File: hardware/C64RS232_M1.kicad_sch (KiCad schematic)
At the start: 9 parts, among them J1 C64 USER PORT, J2 5747844-4, U1 MAX3243EIPWR

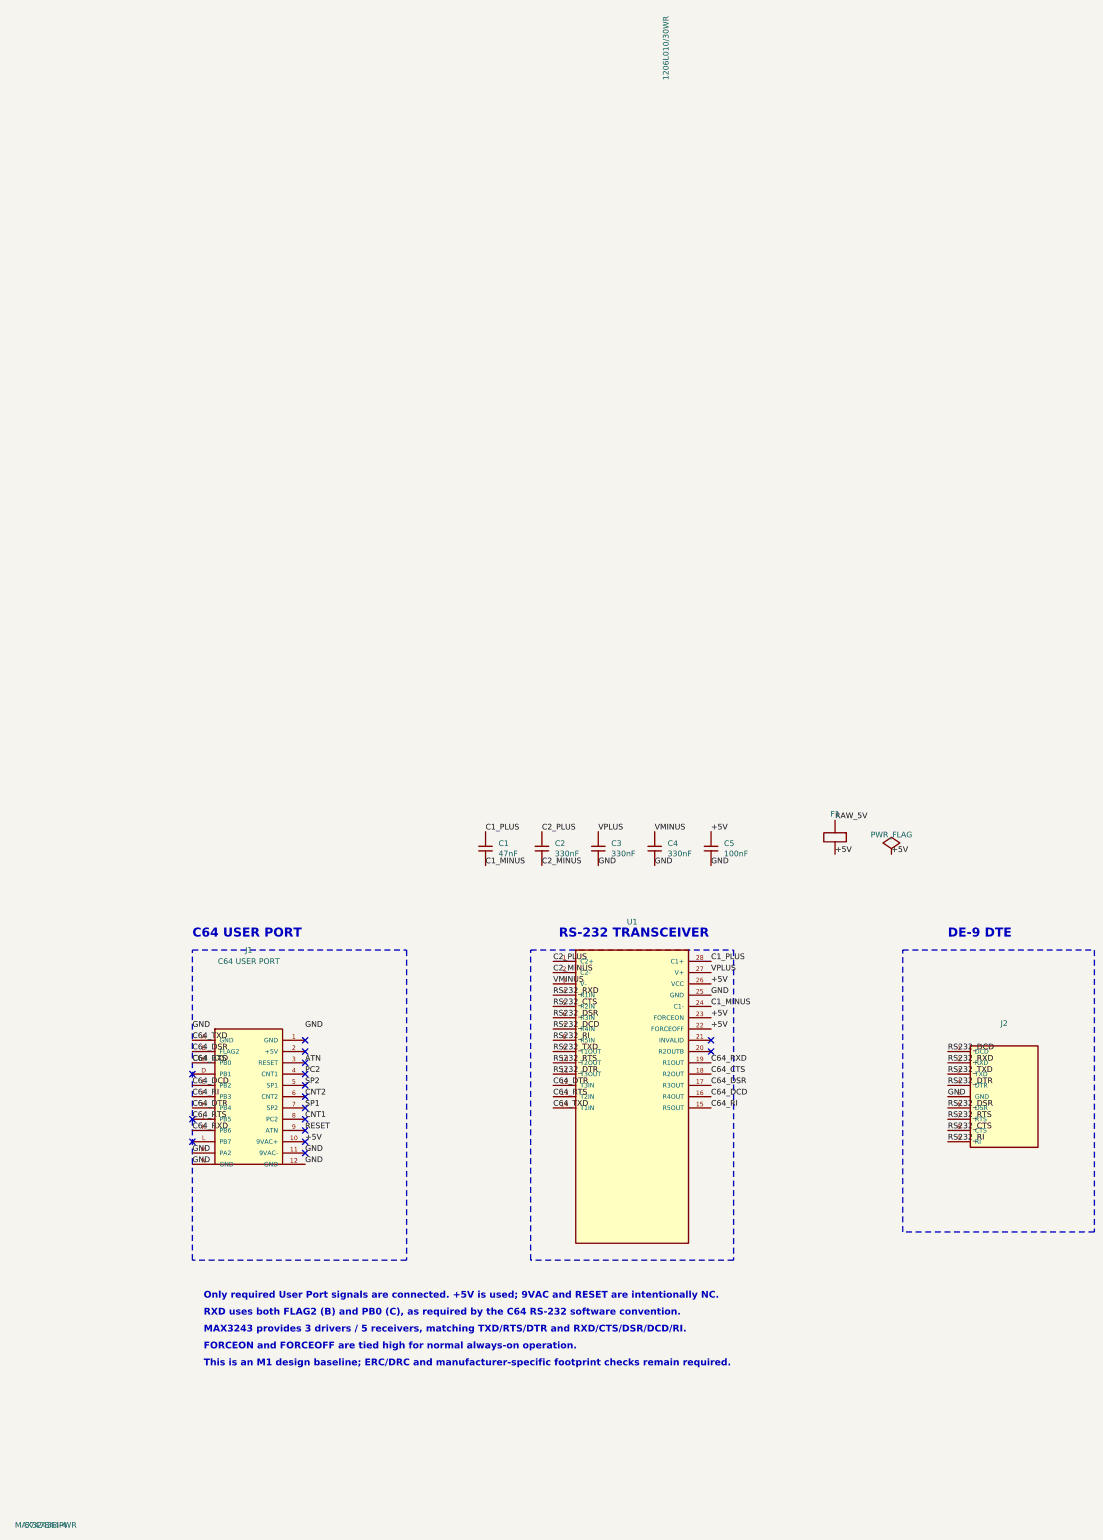
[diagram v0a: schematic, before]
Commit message: Restore electrically connected M1.9 schematic baseline
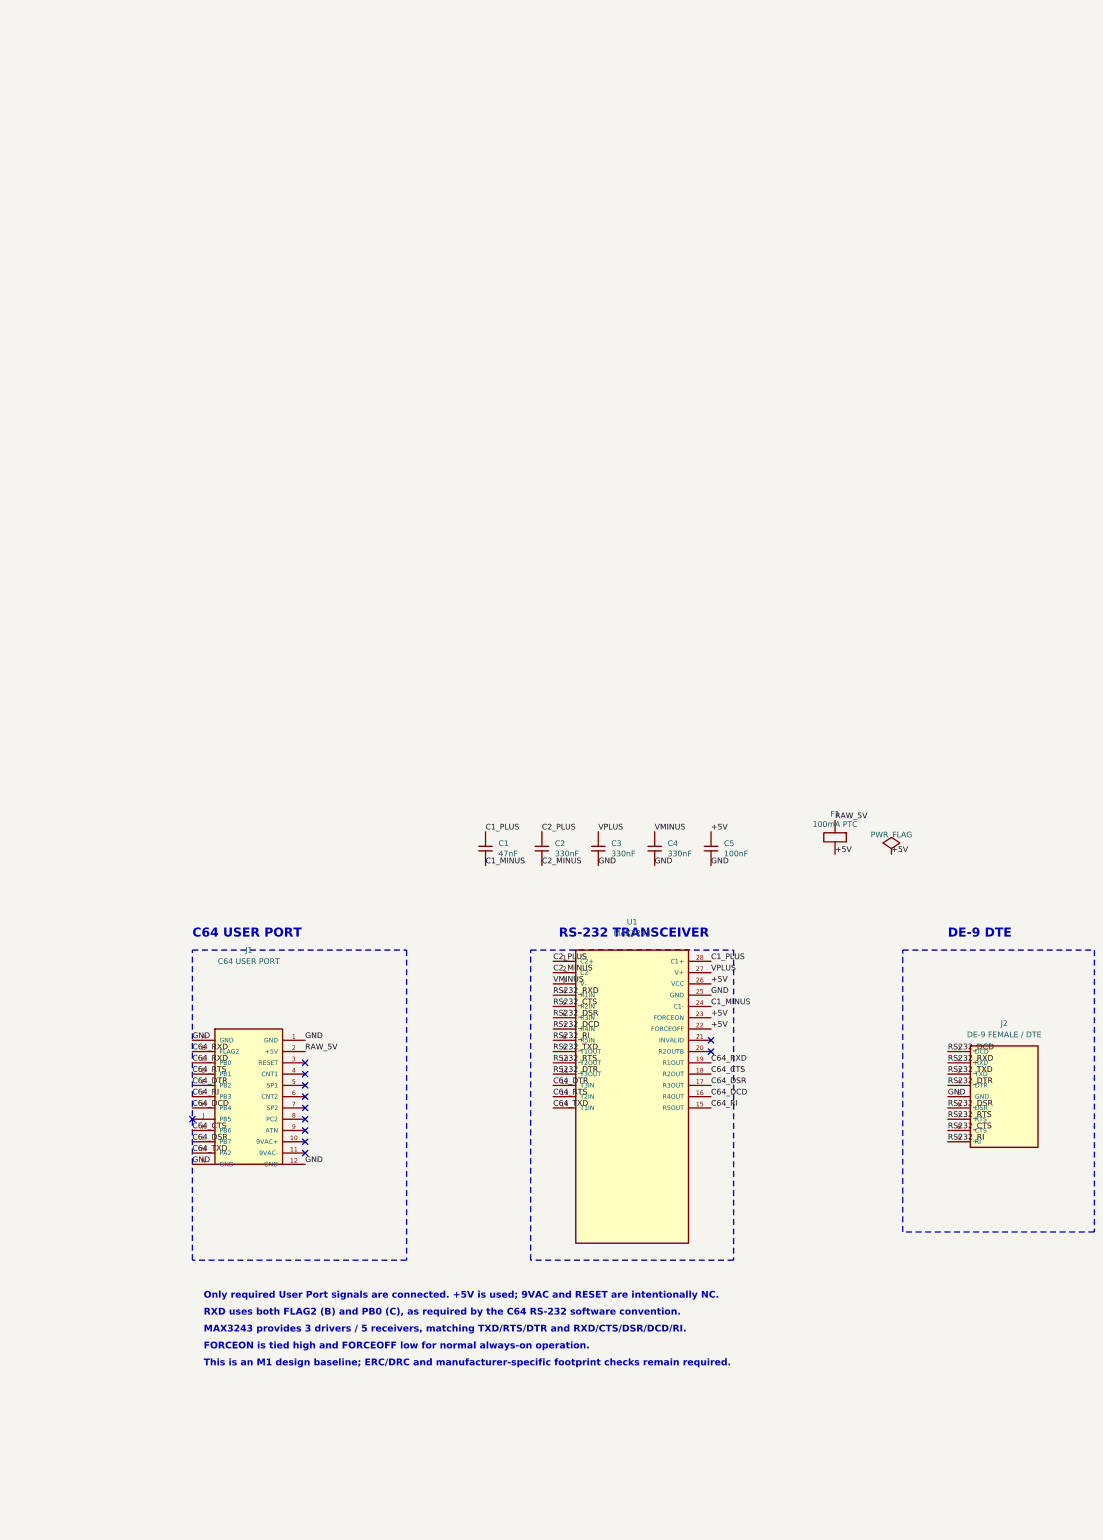
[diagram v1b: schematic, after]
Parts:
- C1, C2, C3, C4, C5: footprint Capacitor_SMD:C_0805_2012Metric_Pad1.18x1.45mm_HandSolder -> (none)
- F1: value 1206L010/30WR -> 100mA PTC; footprint Fuse:Fuse_1206_3216Metric_Pad1.42x1.75mm_HandSolder -> (none)
- J1: footprint C64RS232:C64_User_Port_Edge -> (none)
- J2: value 5747844-4 -> DE-9 FEMALE / DTE; footprint C64RS232:TE_5747844-4 -> (none)
- U1: value MAX3243EIPWR -> MAX3243; footprint Package_SO:TSSOP-28_4.4x9.7mm_P0.65mm -> (none)
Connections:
- net +5V: no longer J1.10 (9VAC+)
- net C64_CTS: no longer J1.C (PB0), U1.19 (R1OUT)
- net C64_DCD: now also J1.H (PB4); no longer J1.E (PB2)
- net C64_DSR: now also J1.L (PB7); no longer J1.B (FLAG2)
- net C64_DTR: now also J1.E (PB2); no longer J1.H (PB4)
- net C64_RTS: now also J1.D (PB1); no longer J1.J (PB5)
- net C64_TXD: now also J1.M (PA2); no longer J1.A (GND)
- net GND: now also J1.1 (GND), J1.A (GND); no longer J1.11 (9VAC-), J1.M (PA2)
- net RAW_5V: now also J1.2 (+5V)
- net ATN: no longer names the net of J1.3 (RESET)
- net CNT1: no longer names the net of J1.8 (PC2)
- net CNT2: no longer names the net of J1.6 (CNT2)
- net PC2: no longer names the net of J1.4 (CNT1)
- net RESET: no longer names the net of J1.9 (ATN)
- net SP1: no longer names the net of J1.7 (SP2)
- net SP2: no longer names the net of J1.5 (SP1)
- new net C64_RXD: J1.B (FLAG2), J1.C (PB0), U1.19 (R1OUT)
- no-connect marks 16 -> 12
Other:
- note added: "FORCEON is tied high and FORCEOFF low for normal always-on operation."
- note removed: "FORCEON and FORCEOFF are tied high for normal always-on operation."

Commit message: Generate M1.10 KiCad schematic baseline
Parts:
- C1, C2, C3, C4, C5: footprint (none) -> Capacitor_SMD:C_0805_2012Metric_Pad1.18x1.45mm_HandSolder
- F1: value 100mA PTC -> 1206L010/30WR; footprint (none) -> Fuse:Fuse_1206_3216Metric_Pad1.42x1.75mm_HandSolder
- J1: footprint (none) -> C64RS232:C64_User_Port_Edge
- J2: value DE-9 FEMALE / DTE -> 5747844-4; footprint (none) -> Connector_Dsub:DSUB-9_Female_Horizontal_P2.77x2.84mm_EdgePinOffset9.40mm_Housed_MountingHolesOffset11.32mm
- U1: value MAX3243 -> MAX3243EIPWR; footprint (none) -> Package_SO:TSSOP-28_4.4x9.7mm_P0.65mm
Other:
- note added: "FORCEON and FORCEOFF are tied high for normal always-on operation."
- note removed: "FORCEON is tied high and FORCEOFF low for normal always-on operation."
